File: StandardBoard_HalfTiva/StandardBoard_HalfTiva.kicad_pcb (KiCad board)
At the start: 2 copper layers, 61 x 99.8 mm, 1 part

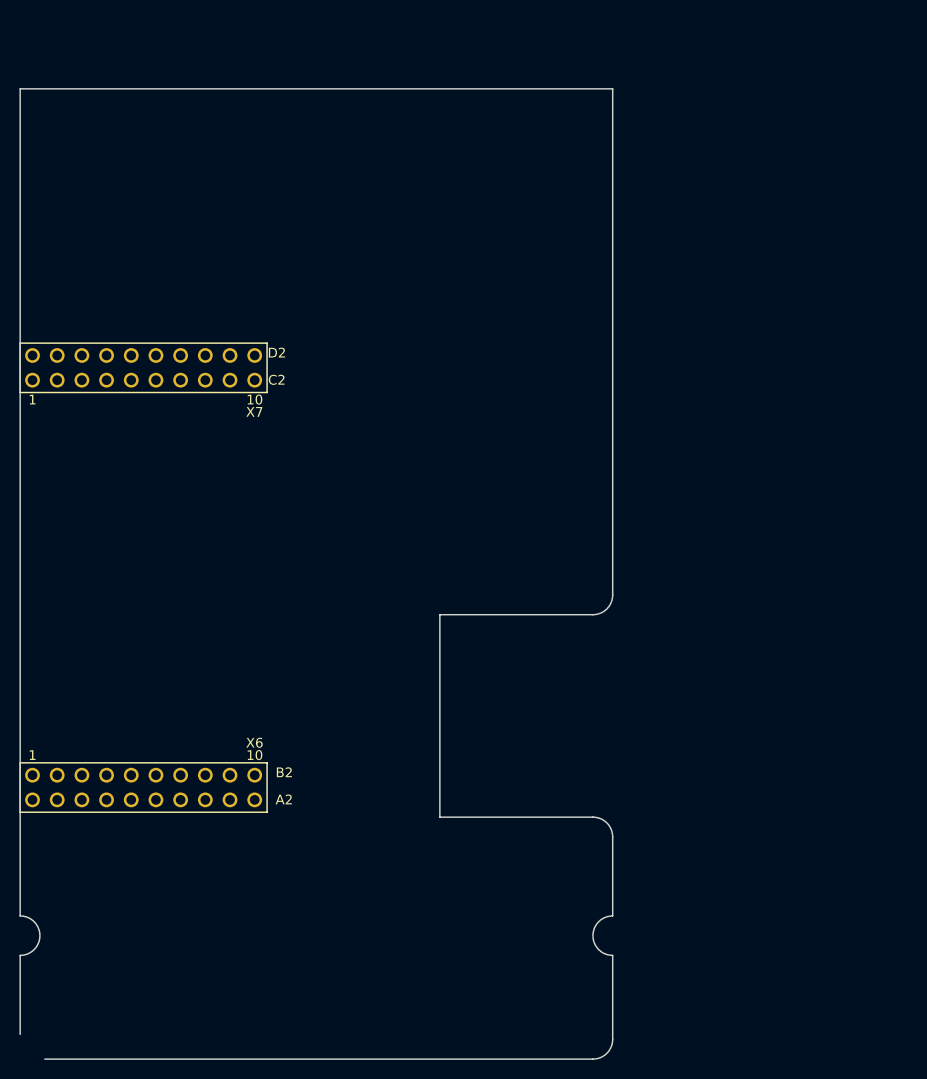
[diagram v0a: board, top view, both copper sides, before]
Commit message: Added silksceen and generated gerbs
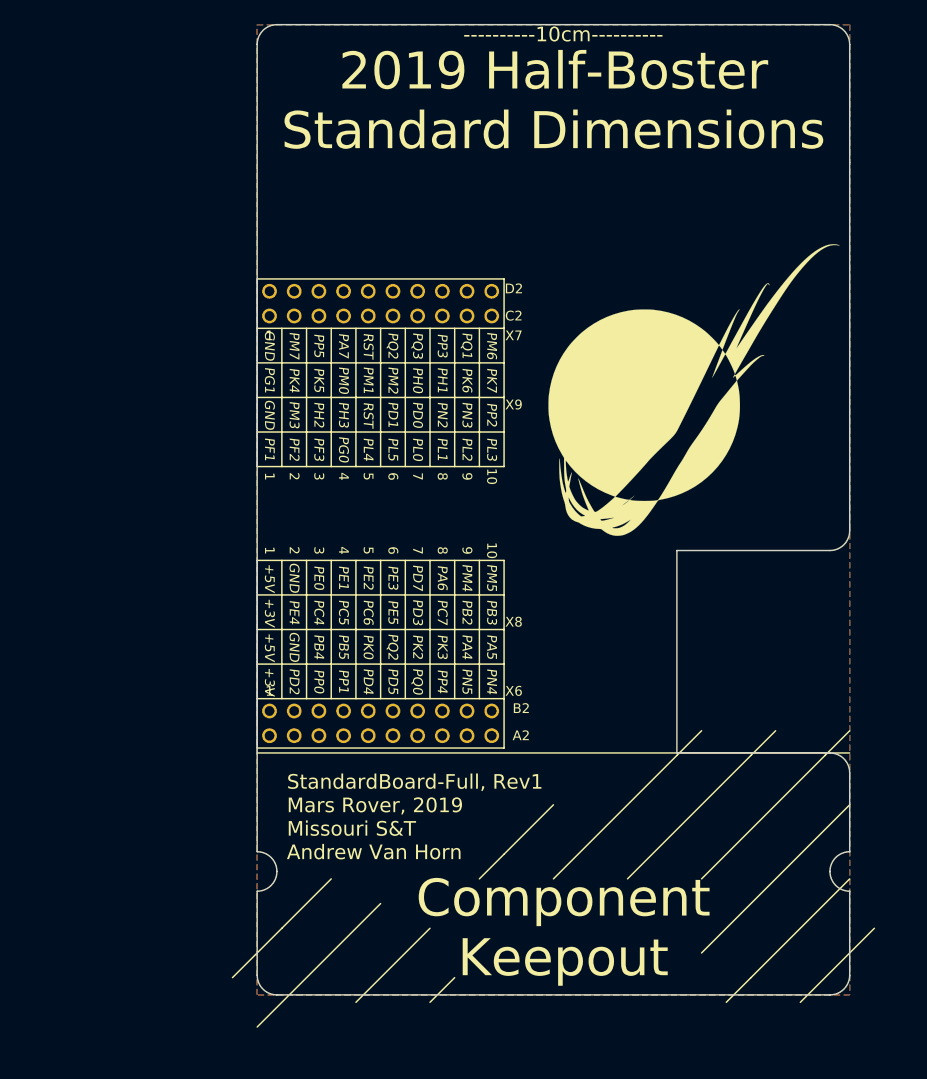
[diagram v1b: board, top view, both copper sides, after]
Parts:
- added G***: LOGO, MRDT_Silkscreens:MRDT_Logo_30mm, F.Cu at (199.9, 81.8)
- moved REF** 25.3 mm to (154.9, 118.6)
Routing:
- added copper zone on B.Cu, net (none)
- added copper zone on F.Cu, net (none)
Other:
- outline, holes or cut-outs redrawn
- board text added: "+3V"
- board text added: "+5V"
- board text added: "----------10cm----------"
- board text added: "-->"
- board text added: "1"
- board text added: "10"
- board text added: "2"
- board text added: "2019 Half-Boster Standard Dimensions"
- board text added: "3"
- board text added: "4"
- board text added: "5"
- board text added: "6"
- board text added: "7"
- board text added: "8"
- board text added: "9"
- board text added: "A2"
- board text added: "B2"
- board text added: "Board May Extend This Way"
- board text added: "C2"
- board text added: "Component Keepout"
- board text added: "D2"
- board text added: "GND"
- board text added: "PA4"
- board text added: "PA5"
- board text added: "PA6"
- board text added: "PA7"
- board text added: "PB2"
- board text added: "PB3"
- board text added: "PB4"
- board text added: "PB5"
- board text added: "PC4"
- board text added: "PC5"
- board text added: "PC6"
- board text added: "PC7"
- board text added: "PD0"
- board text added: "PD1"
- board text added: "PD2"
- board text added: "PD3"
- board text added: "PD4"
- board text added: "PD5"
- board text added: "PD7"
- board text added: "PE0"
- board text added: "PE1"
- board text added: "PE2"
- board text added: "PE3"
- board text added: "PE4"
- board text added: "PE5"
- board text added: "PF1"
- board text added: "PF2"
- board text added: "PF3"
- board text added: "PG0"
- board text added: "PG1"
- board text added: "PH0"
- board text added: "PH1"
- board text added: "PH2"
- board text added: "PH3"
- board text added: "PK0"
- board text added: "PK2"
- board text added: "PK3"
- board text added: "PK4"
- board text added: "PK5"
- board text added: "PK6"
- board text added: "PK7"
- board text added: "PL0"
- board text added: "PL1"
- board text added: "PL2"
- board text added: "PL3"
- board text added: "PL4"
- board text added: "PL5"
- board text added: "PM0"
- board text added: "PM1"
- board text added: "PM2"
- board text added: "PM3"
- board text added: "PM4"
- board text added: "PM5"
- board text added: "PM6"
- board text added: "PM7"
- board text added: "PN2"
- board text added: "PN3"
- board text added: "PN4"
- board text added: "PN5"
- board text added: "PP0"
- board text added: "PP1"
- board text added: "PP2"
- board text added: "PP3"
- board text added: "PP4"
- board text added: "PP5"
- board text added: "PQ0"
- board text added: "PQ1"
- board text added: "PQ2"
- board text added: "PQ3"
- board text added: "RST"
- board text added: "StandardBoard-Full, Rev1 Mars Rover, 2019 Missouri S&T Andrew Van Horn"
- board text added: "X6"
- board text added: "X7"
- board text added: "X8"
- board text added: "X9"
